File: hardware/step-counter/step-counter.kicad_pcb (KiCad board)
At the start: 4 copper layers, 50 parts, among them J1 Conn_01x10_Male, J2 Conn_01x14_Male, J3 Conn_01x10_Male, J4 Conn_Power, U1 74HC161, U10 74HC161, U11 74LVC1G02, U12 74LVC2G04, U13 74HC4024, U14 74LVC1G332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

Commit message: Updated PCBs
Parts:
- R1, R2, R3, R4, R5, R6, U2: moved to B.Cu
- moved J1 185.7 mm to (264.2, 53.3)
- moved U3 184.9 mm to (224.2, 79.4), turned to -90 degrees
- moved U1 172.2 mm to (211.5, 79.4), turned to -90 degrees
- moved U10 163.3 mm to (202.6, 54.6)
- moved U13 163.3 mm to (223.5, 62.2)
- moved U7 163.3 mm to (217.8, 54.0)
- moved U8 163.3 mm to (210.8, 54.0)
- moved U9 159.9 mm to (189.9, 87.0), turned to 90 degrees
- moved U6 156.7 mm to (185.4, 87.0), turned to 90 degrees
- moved J3 139.2 mm to (198.1, 38.1), turned to 90 degrees
- moved U5 133.4 mm to (189.9, 75.6), turned to -90 degrees
- moved U4 116.3 mm to (198.8, 87.0), turned to 90 degrees
- moved U11 115.6 mm to (194.3, 87.0), turned to 90 degrees
- moved J2 88.5 mm to (195.6, 99.1), turned to 90 degrees
- moved U2 52.2 mm to (179.1, 52.1), turned to 180 degrees
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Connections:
- J2 pad 10: /Q2 -> /Q3
- J2 pad 11: /Q3 -> /Q2
- J2 pad 12: /Q4 -> /Q1
- J2 pad 13: /Q5 -> /Q0
- J2 pad 8: /Q0 -> /Q5
- J2 pad 9: /Q1 -> /Q4
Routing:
- net /~{CLK}: track 35.6 -> 21.7 mm
- net /~{RESET}: track 58.5 -> 48.4 mm

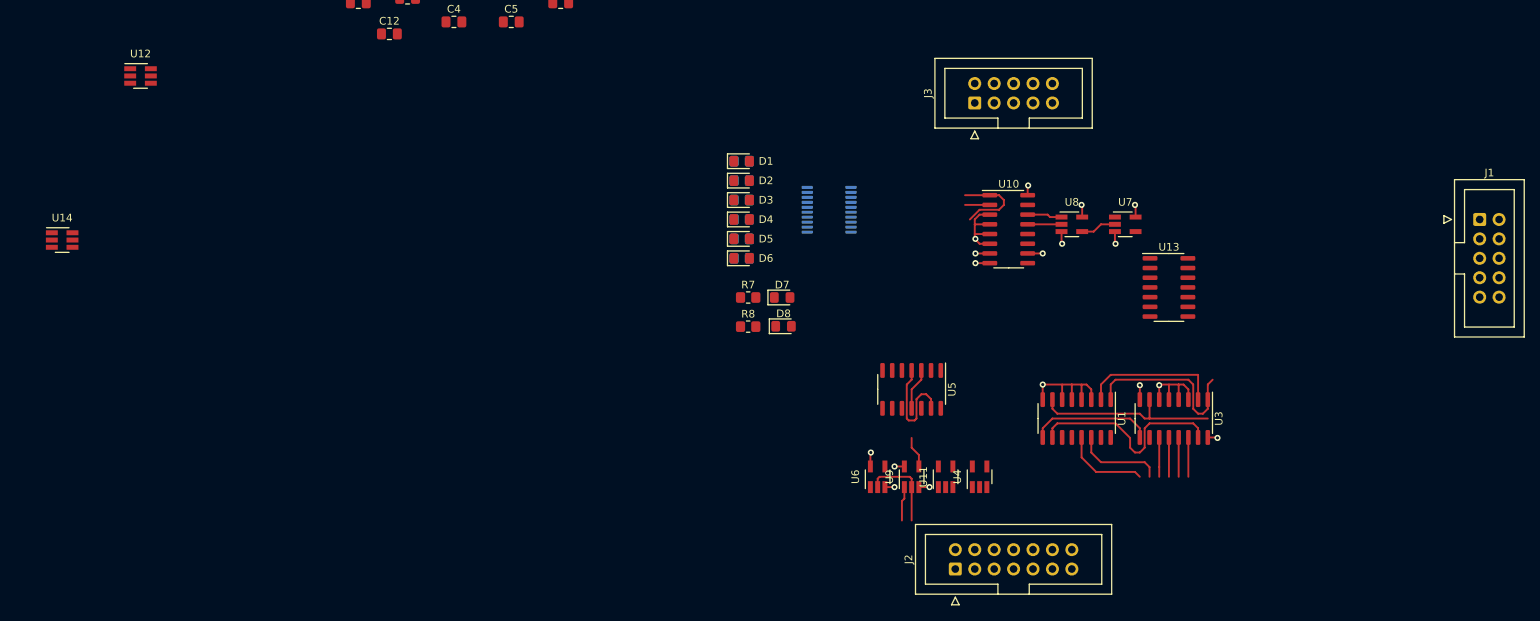
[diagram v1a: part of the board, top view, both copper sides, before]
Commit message: Updated opcode and step counter PCBs
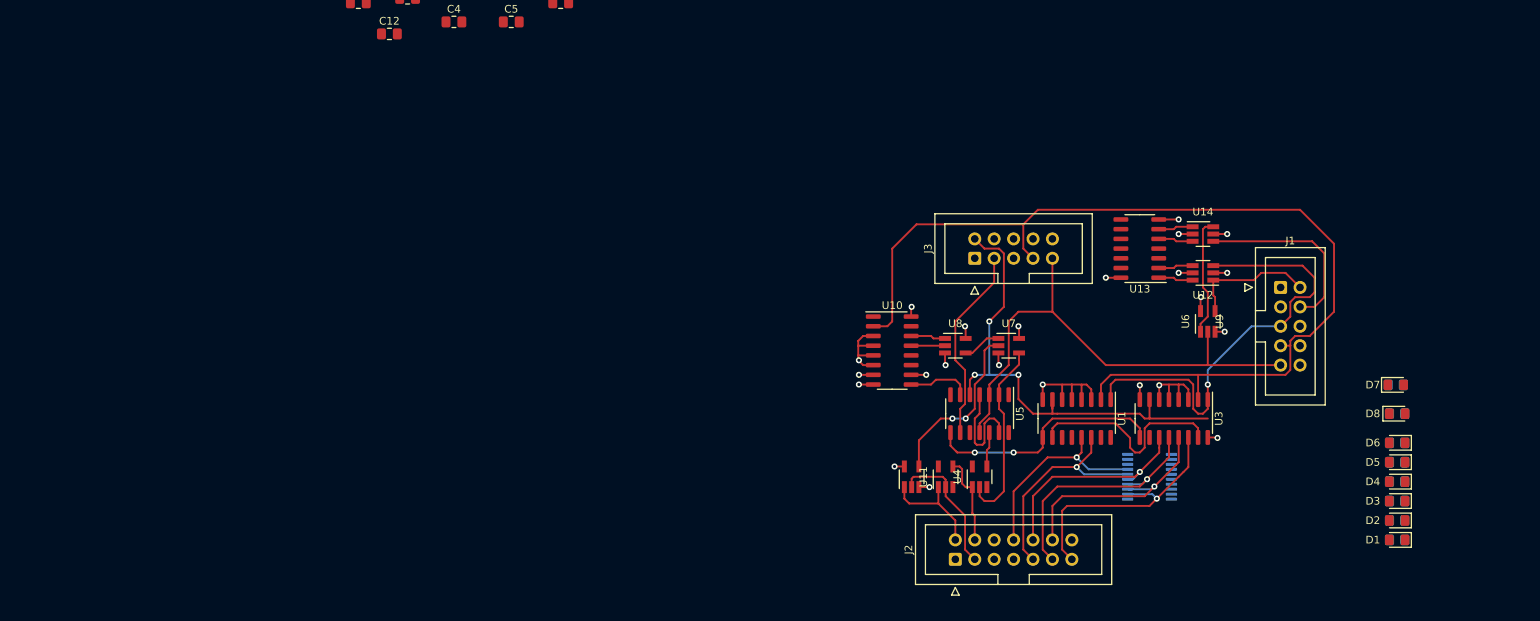
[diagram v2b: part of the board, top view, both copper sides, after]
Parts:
- R7, R8: moved to B.Cu
- moved U14 149.2 mm to (228.0, 55.2)
- moved U12 141.3 mm to (228.0, 60.3), turned to 180 degrees
- moved D1 99.0 mm to (253.4, 95.2), turned to 180 degrees
- moved R1 99.0 mm to (253.4, 95.2), turned to 180 degrees
- moved D2 96.6 mm to (253.4, 92.7), turned to 180 degrees
- moved R2 96.6 mm to (253.4, 92.7), turned to 180 degrees
- moved D3 94.3 mm to (253.4, 90.2), turned to 180 degrees
- moved R3 94.3 mm to (253.4, 90.2), turned to 180 degrees
- moved D4 92.3 mm to (253.4, 87.6), turned to 180 degrees
- moved R4 92.3 mm to (253.4, 87.6), turned to 180 degrees
- moved D5 90.6 mm to (253.4, 85.1), turned to 180 degrees
- moved R5 90.6 mm to (253.4, 85.1), turned to 180 degrees
- moved D6 89.1 mm to (253.4, 82.5), turned to 180 degrees
- moved R6 89.1 mm to (253.4, 82.5), turned to 180 degrees
- moved R8 85.6 mm to (253.4, 78.7)
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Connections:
- U14 pad 1: /LEN1 -> Net-(U13-Pad6)
- U14 pad 3: Net-(U13-Pad6) -> Net-(U13-Pad5)
- U14 pad 6: Net-(U13-Pad5) -> /LEN1
- U6 pad 1: /CLK -> /LEN1
- U6 pad 2: /LEN1 -> /CLK
- U7 pad 1: /~{LEN4} -> Net-(U8-Pad4)
- U7 pad 2: Net-(U7-Pad2) -> /~{LEN4}
- U8 pad 4: Net-(U7-Pad2) -> Net-(U8-Pad4)
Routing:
- net /~{CLK}: track 21.7 -> 131.0 mm
- net /CLK: track 5.48 -> 66.4 mm
- net /STEP_DONE: track 24.5 -> 64.4 mm, vias 0 -> 3
- net /Q0: track 5.15 -> 33.7 mm, vias 0 -> 1
- net /Q2: track 5.15 -> 32.4 mm, vias 0 -> 1
- net /OP_DONE: track 0.00 -> 25.7 mm
- net /Q1: track 5.15 -> 30.2 mm, vias 0 -> 1
- net /~{RESET}: track 48.4 -> 73.3 mm, vias 0 -> 1
- net /LAST_SUBSTEP: track 0.00 -> 24.6 mm
- net /IMM_PC_OUT_S~{P}: track 0.00 -> 24.6 mm
- net /Q3: track 5.15 -> 28.6 mm, vias 0 -> 1
- net /LEN1: track 11.2 -> 33.3 mm
- net /~{LEN4}: track 4.12 -> 22.7 mm, vias 0 -> 2
- net /Q4: track 11.6 -> 29.1 mm, vias 0 -> 1
- net /BUS_CLK: track 0.00 -> 16.7 mm
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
